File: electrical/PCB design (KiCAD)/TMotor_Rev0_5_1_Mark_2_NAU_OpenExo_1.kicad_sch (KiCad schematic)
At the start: 13 parts, among them U5 TXU0104PWR, U6 TXU0304-Q1, U7 DEV-16771

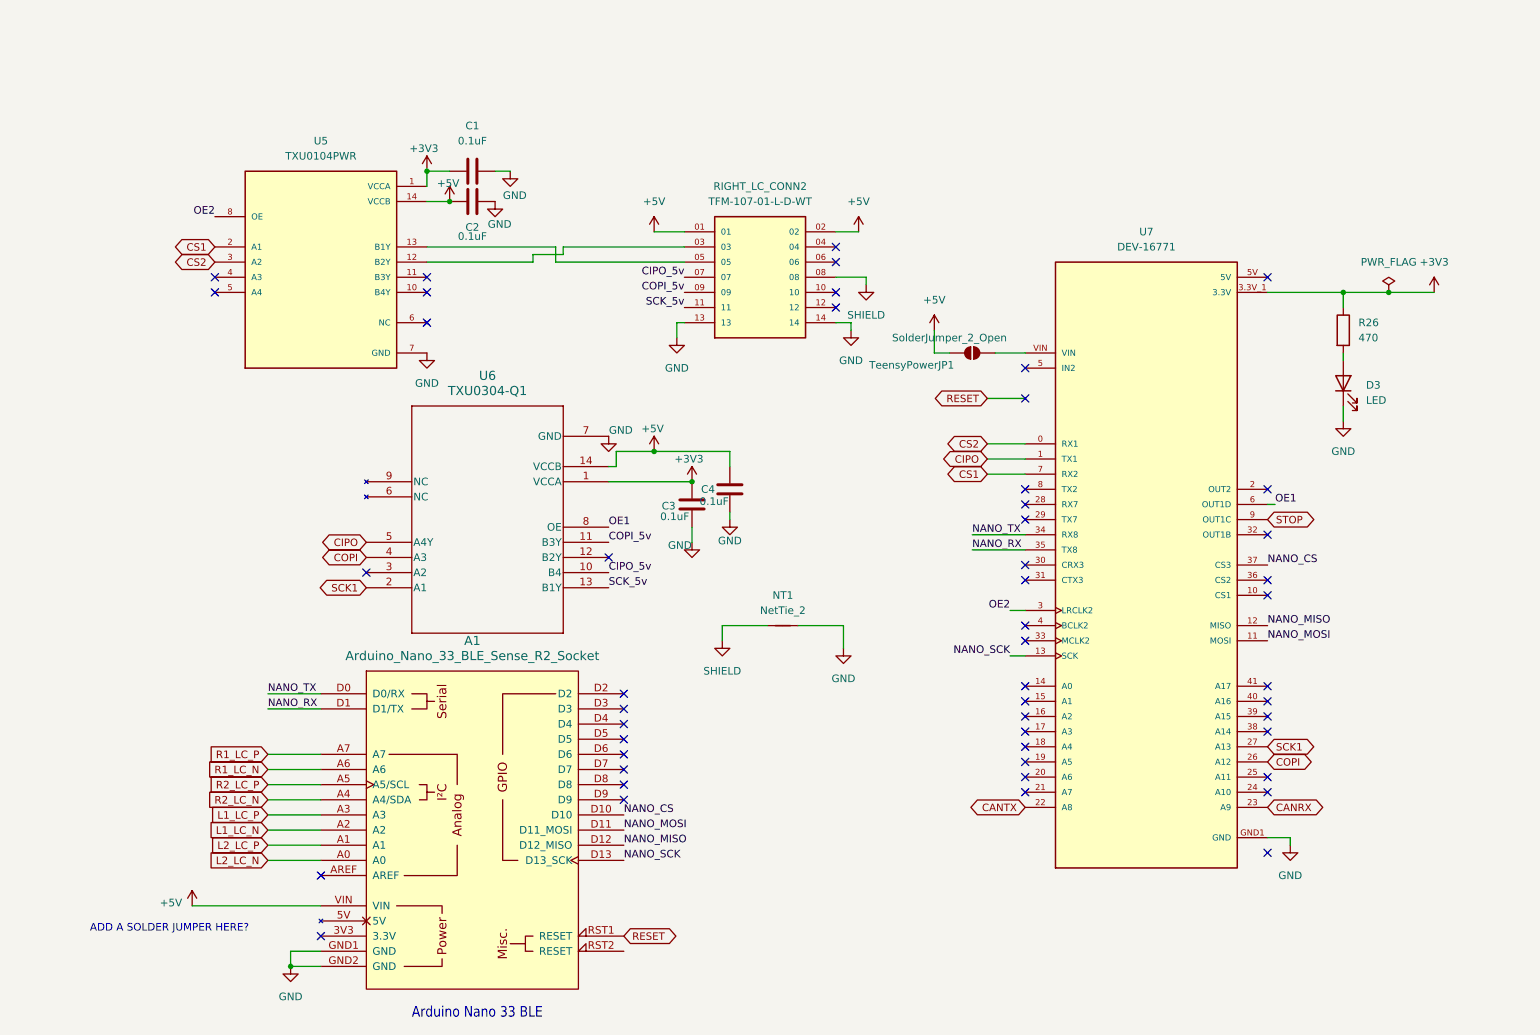
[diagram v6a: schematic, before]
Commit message: fix modularize python script for ble.py and sensors.py (main and plotting-csv not done
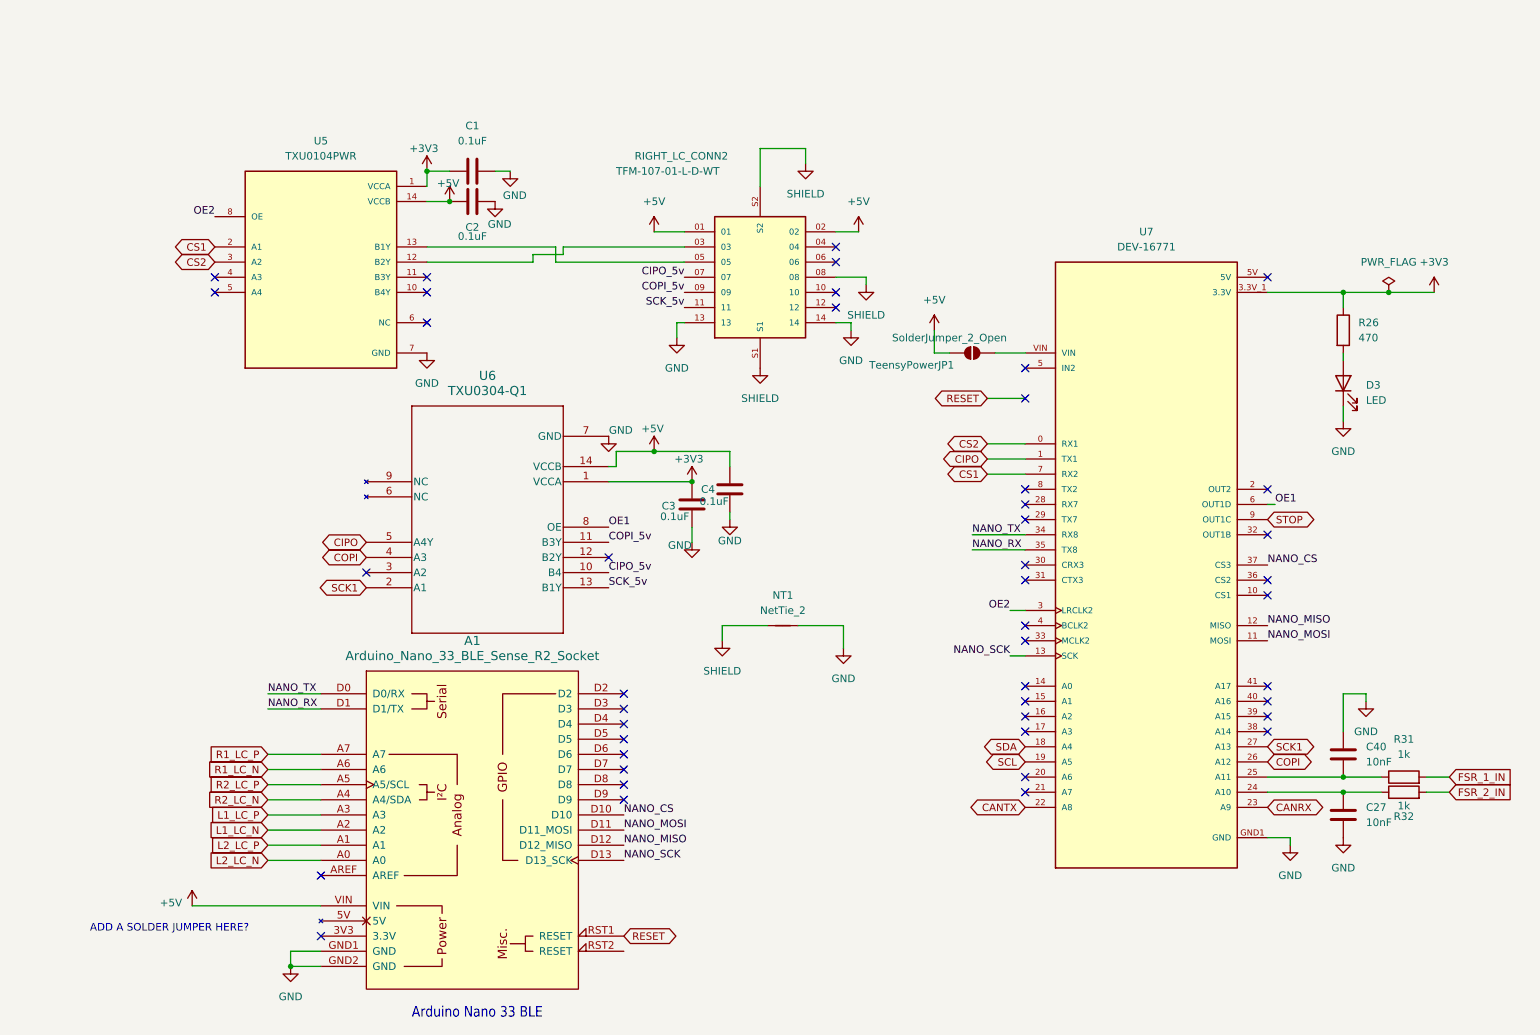
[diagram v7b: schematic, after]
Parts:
- added C27, C40: 10nF, Capacitor_SMD:C_0805_2012Metric_Pad1.18x1.45mm_HandSolder, symbol Device:C
- added R31, R32: 1k, Resistor_SMD:R_0805_2012Metric_Pad1.20x1.40mm_HandSolder, symbol Device:R
- RIGHT_LC_CONN2: footprint ISDF connector:SAMTEC_TFM-107-01-L-D-WT -> TFM-107-01-L-D-WT:SAMTEC_TFM-107-01-L-D-WT
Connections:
- net GND: now also C27.2, C40.1
- net SHIELD: now also RIGHT_LC_CONN2.S1, RIGHT_LC_CONN2.S2
- net SDA: now reaches U7.18 (A4)
- net SCL: now reaches U7.19 (A5)
- net at U7.24 (A10): now also C27.1, R32.1
- net at U7.25 (A11): now also C40.2, R31.1
- new net FSR_1_IN: R31.2
- new net FSR_2_IN: R32.2
- no-connect marks 50 -> 45
